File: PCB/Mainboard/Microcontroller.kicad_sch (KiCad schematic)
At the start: 21 parts, among them J3 PinHeader 02x03, J7 JST-PH 01x08, Q2 N-channel, U6 ATMEGA328PB-AU, U7 M24256 EEPROM, Y1 8MHz

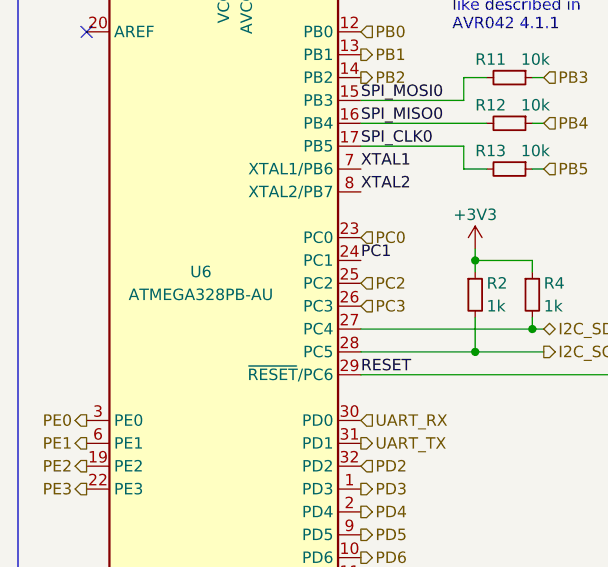
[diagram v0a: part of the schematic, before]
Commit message: Update schematic and lay-out
- Swap out CP2102N, ATmega328PB and CP with new Kicad 6 symbol
- Correct all links to point to new zoudio_symbols and zoudio_footprint libraries
- Lay-out updated, only antenna is left to update.
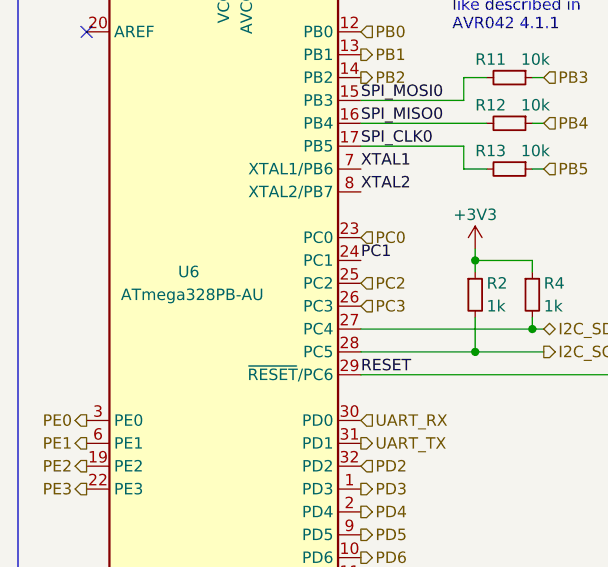
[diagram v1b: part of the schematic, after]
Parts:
- removed U6: ATMEGA328PB-AU, Package_QFP:TQFP-32_7x7mm_P0.8mm, symbol MCU_Microchip_ATmega:ATmega328PB-AU
- added U6: ATmega328PB-AU, Package_QFP:TQFP-32_7x7mm_P0.8mm, symbol MCU_Microchip_ATmega:ATmega328PB-A
- U7: symbol ZOUDIO-symbols:EEPROM_TSSOP -> zoudio_symbols:EEPROM_TSSOP
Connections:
- net +3V3: now also U6.18 (AVCC), U6.4 (VCC)
- net GND: now also U6.21 (GND), U6.5 (GND)
- net I2C_SCL: now also U6.28 (PC5)
- net I2C_SDA: now also U6.27 (PC4)
- net PB0: now also U6.12 (PB0)
- net PB1: now also U6.13 (PB1)
- net PB2: now also U6.14 (PB2)
- net PC0: now also U6.23 (PC0)
- net PC1: now also U6.24 (PC1)
- net PC2: now also U6.25 (PC2)
- net PC3: now also U6.26 (PC3)
- net PD2: now also U6.32 (PD2)
- net PD3: now also U6.1 (PD3)
- net PD4: now also U6.2 (PD4)
- net PD5: now also U6.9 (PD5)
- net PD6: now also U6.10 (PD6)
- net PD7: now also U6.11 (PD7)
- net PE0: now also U6.3 (PE0)
- net PE1: now also U6.6 (PE1)
- net PE2: now also U6.19 (PE2)
- net PE3: now also U6.22 (PE3)
- net RESET: now also U6.29 (~{RESET}/PC6)
- net SPI_CLK0: now also U6.17 (PB5)
- net SPI_MISO0: now also U6.16 (PB4)
- net SPI_MOSI0: now also U6.15 (PB3)
- net UART_RX: now also U6.30 (PD0)
- net UART_TX: now also U6.31 (PD1)
- net XTAL1: now also U6.7 (XTAL1/PB6)
- net XTAL2: now also U6.8 (XTAL2/PB7)

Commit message: Add buck, change some part values
Add new buck in schematic and layout.
Modify BT module footprint,
Change power led resistor from 1k to 100R
Change 4.7u TAS resistors to 10u (consolidation)
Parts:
- added TP1: TestPoint, TestPoint:TestPoint_Pad_D1.0mm, symbol Connector:TestPoint
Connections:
- net PE1: now also TP1.1
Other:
- note added: "Pin previously used for VREG_SLEEP"
- note added: "Testpoint for debug"
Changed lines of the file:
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@@
+    (stroke (width 0) (type default) (color 0 0 0 0))
+  )
+  (polyline (pts (xy 204.47 93.98) (xy 204.47 106.68))
     (stroke (width 0) (type default) (color 0 0 0 0))
   )
@@
     (stroke (width 0) (type default) (color 0 0 0 0))
   )
+  (wire (pts (xy 209.55 97.79) (xy 210.82 97.79))
+    (stroke (width 0) (type default) (color 0 0 0 0))
+  )
   (wire (pts (xy 139.7 97.79) (xy 139.7 99.06))
     (stroke (width 0) (type default) (color 0 0 0 0))
@@
     (stroke (width 0) (type default) (color 0 0 0 0))
   )
+  (polyline (pts (xy 226.06 106.68) (xy 204.47 106.68))
+    (stroke (width 0) (type default) (color 0 0 0 0))
+  )
   (polyline (pts (xy 67.31 144.78) (xy 67.31 49.53))
     (stroke (width 0) (type default) (color 0 0 0 0))
@@
     (stroke (width 0) (type default) (color 0 0 0 0))
   )
+  (polyline (pts (xy 226.06 93.98) (xy 226.06 106.68))
+    (stroke (width 0) (type default) (color 0 0 0 0))
+  )
   (wire (pts (xy 209.55 130.81) (xy 209.55 133.35))
     (stroke (width 0) (type default) (color 0 0 0 0))
@@
     (stroke (width 0) (type default) (color 0 0 0 0))
   )
+  (polyline (pts (xy 204.47 93.98) (xy 226.06 93.98))
+    (stroke (width 0) (type default) (color 0 0 0 0))
+  )
   (polyline (pts (xy 153.67 49.53) (xy 153.67 144.78))
     (stroke (width 0) (type default) (color 0 0 0 0))
@@
     (effects (font (size 1.27 1.27)) (justify left bottom))
   )
+  (text "Testpoint for debug" (at 204.47 93.98 0)
+    (effects (font (size 1.27 1.27)) (justify left bottom))
+  )
   (text "Expansion header" (at 160.02 111.76 0)
+    (effects (font (size 1.27 1.27)) (justify left bottom))
+  )
+  (text "Pin previously used \nfor VREG_SLEEP" (at 205.74 105.41 0)
     (effects (font (size 1.27 1.27)) (justify left bottom))
   )
@@
     (effects (font (size 1.27 1.27)) (justify left bottom))
   )
+  (label "PE1" (at 74.93 114.3 180)
+    (effects (font (size 1.27 1.27)) (justify right bottom))
+  )
   (label "RESET" (at 200.66 133.35 180)
     (effects (font (size 1.27 1.27)) (justify right bottom))
@@
     (effects (font (size 1.27 1.27)) (justify right bottom))
   )
+  (label "PE1" (at 209.55 97.79 180)
+    (effects (font (size 1.27 1.27)) (justify right bottom))
+  )
   (label "I2C_SCL" (at 218.44 135.89 180)
     (effects (font (size 1.27 1.27)) (justify right bottom))
@@
   (hierarchical_label "UART_TX" (shape output) (at 105.41 114.3 0)
     (effects (font (size 1.27 1.27)) (justify left))
-  )
-  (hierarchical_label "PE1" (shape output) (at 74.93 114.3 180)
-    (effects (font (size 1.27 1.27)) (justify right))
   )
   (hierarchical_label "PC2" (shape input) (at 105.41 96.52 0)
@@
     (pin "9")
   )
+  (symbol (lib_id "Connector:TestPoint") (at 210.82 97.79 270) (unit 1)
+    (in_bom yes) (on_board yes) (fields_autoplaced)
+    (property "Reference" "TP1" (id 0) (at 215.9 96.5199 90)
+      (effects (font (size 1.27 1.27)) (justify left))
+    )
+    (property "Value" "TestPoint" (id 1) (at 215.9 99.0599 90)
+      (effects (font (size 1.27 1.27)) (justify left))
+    )
+    (property "Footprint" "TestPoint:TestPoint_Pad_D1.0mm" (id 2) (at 210.82 102.87 0)
+      (effects (font (size 1.27 1.27)) hide)
+    )
+    (property "Datasheet" "~" (id 3) (at 210.82 102.87 0)
+      (effects (font (size 1.27 1.27)) hide)
+    )
+    (property "Config" "dnp" (id 4) (at 210.82 97.79 90)
+      (effects (font (size 1.27 1.27)) hide)
+    )
+    (pin "1")
+  )
 )

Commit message: Mainboard: update symbol fields for bom export
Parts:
- C34, C35: Partnumber 0603B104J500CT -> C0603C180K8GACTU
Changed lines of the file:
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@@
       (effects (font (size 1.27 1.27)) hide)
     )
-    (property "Partnumber" "0603B104J500CT" (id 5) (at 222.25 66.04 0)
+    (property "Partnumber" "C0603C180K8GACTU" (id 5) (at 222.25 66.04 0)
       (effects (font (size 1.27 1.27)) hide)
     )
@@
       (effects (font (size 1.27 1.27)) hide)
     )
-    (property "Partnumber" "0603B104J500CT" (id 5) (at 232.41 66.04 0)
+    (property "Partnumber" "C0603C180K8GACTU" (id 5) (at 232.41 66.04 0)
       (effects (font (size 1.27 1.27)) hide)
     )

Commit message: Remove DNP from J3 config field, add partnumber
Header is currently populated in assembly
Add manufacturer and partnumber field
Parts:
- J3: Config dnp -> (none); Manufacturer (none) -> Metz; Partnumber (none) -> PR20203VBDN
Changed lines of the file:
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@@
     )
     (property "Function" "ICSP" (id 4) (at 180.34 99.06 0))
-    (property "Config" "dnp" (id 5) (at 180.34 101.6 0))
+    (property "Config" "" (id 5) (at 180.34 101.6 0))
+    (property "Manufacturer" "Metz" (id 6) (at 179.07 91.44 0)
+      (effects (font (size 1.27 1.27)) hide)
+    )
+    (property "Partnumber" "PR20203VBDN" (id 7) (at 179.07 91.44 0)
+      (effects (font (size 1.27 1.27)) hide)
+    )
     (pin "1")
     (pin "2")
